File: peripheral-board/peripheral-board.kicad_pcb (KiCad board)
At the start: 2 copper layers, 110 x 45 mm, 20 parts, among them J1 Power, J2 Arduino Ports, J3 4WD controller, J4 Head, J5 LED1, J6 LED2, M1 UsbToUartX2, Q1 IRLR8113, Q2 IRLR8113

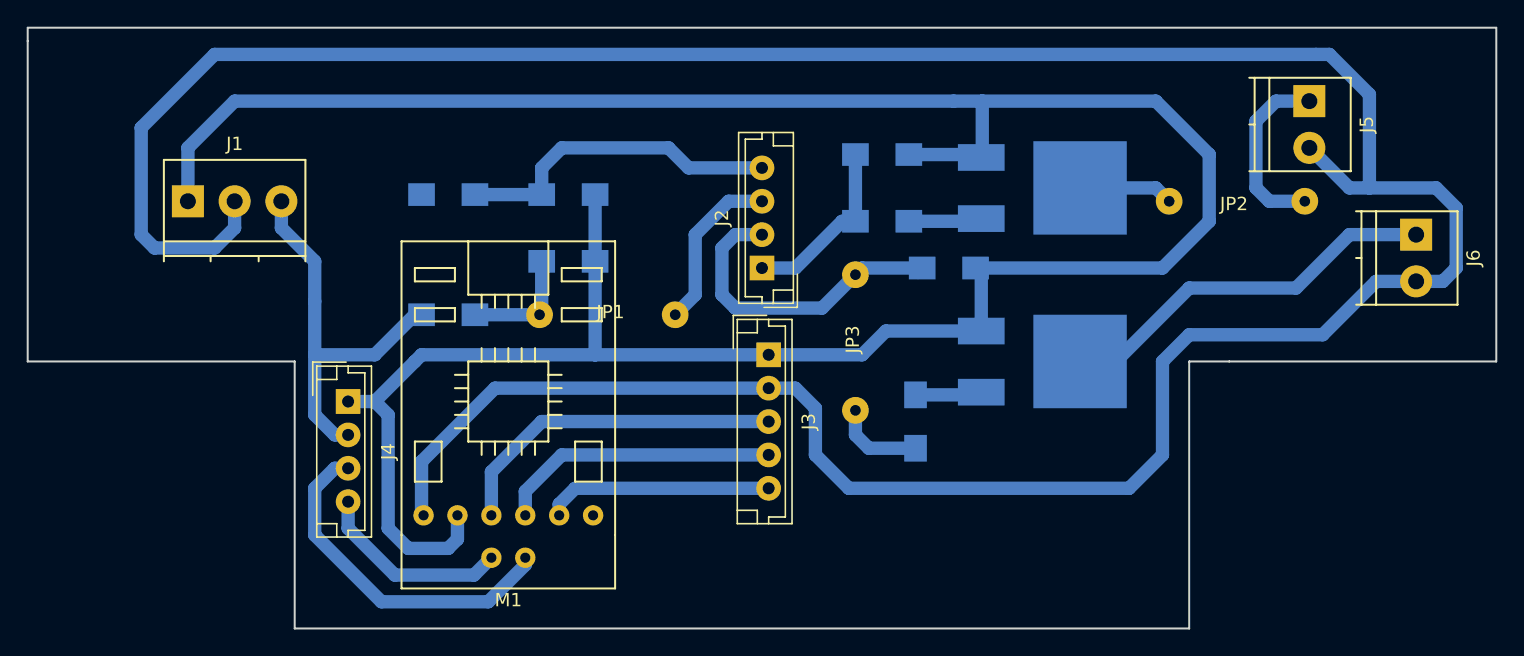
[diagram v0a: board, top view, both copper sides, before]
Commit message: Terminal blocks were fixed
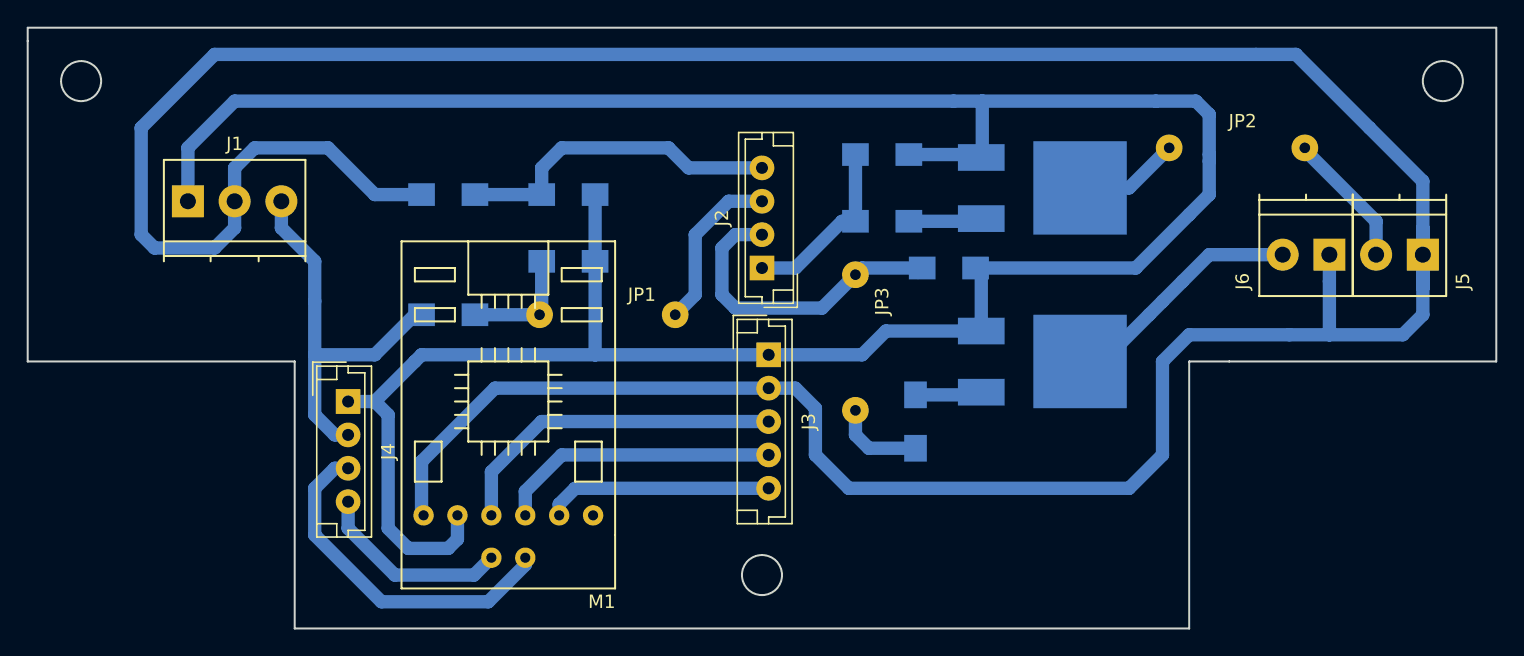
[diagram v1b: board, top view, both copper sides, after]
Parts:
- moved J5 14.3 mm to (204.5, 67.0), turned to 180 degrees
- moved J6 6.67 mm to (197.5, 67.0), turned to 180 degrees
- moved JP2 4.00 mm to (185.5, 59.0)
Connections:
- J5 pad 1: Net-(J5-Pad1) -> +5V
- J5 pad 2: +5V -> Net-(J5-Pad2)
- J6 pad 1: Net-(J6-Pad1) -> +5V
- J6 pad 2: +5V -> Net-(J6-Pad2)
- JP2 pad 2: Net-(J5-Pad1) -> Net-(J5-Pad2)
- M1 pad 1: Net-(M1-Pad1) -> (no net)
- Q2 pad 2: Net-(J6-Pad1) -> Net-(J6-Pad2)
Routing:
- net Net-(J6-Pad1): track 29.8 -> 0.00 mm
- net Net-(J6-Pad2): track 0.00 -> 21.8 mm
- net +5V: track 237.9 -> 255.3 mm
- net Net-(J5-Pad1): track 13.7 -> 0.00 mm
- net Net-(J5-Pad2): track 0.00 -> 10.2 mm
- net Net-(JP2-Pad1): track 7.09 -> 7.92 mm
- net GND: track 203.1 -> 203.7 mm
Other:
- outline, holes or cut-outs redrawn
